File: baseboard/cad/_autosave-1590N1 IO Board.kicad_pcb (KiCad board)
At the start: 4 copper layers, 58 x 77 mm, 105 parts, among them J1 DC POWER JACK, J10 2P_HEADER, J11 2P_HEADER, J12 6-440054-2, J13 6-440054-2, J16 Conn_01x04_Pin, J17 6-440054-2, J18 6-440054-2, J2 1/4" JACK, STEREO, J3 6-440054-2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

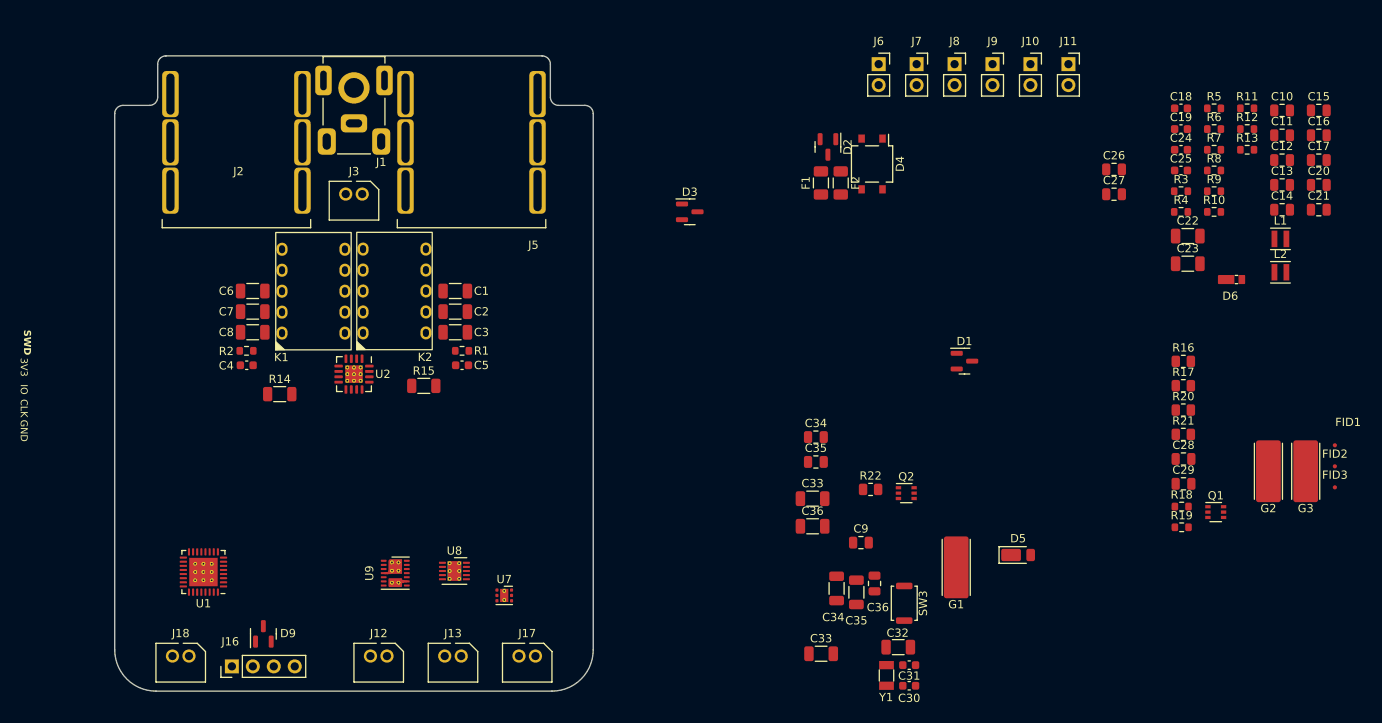
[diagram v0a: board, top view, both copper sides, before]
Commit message: updated schematic page setup
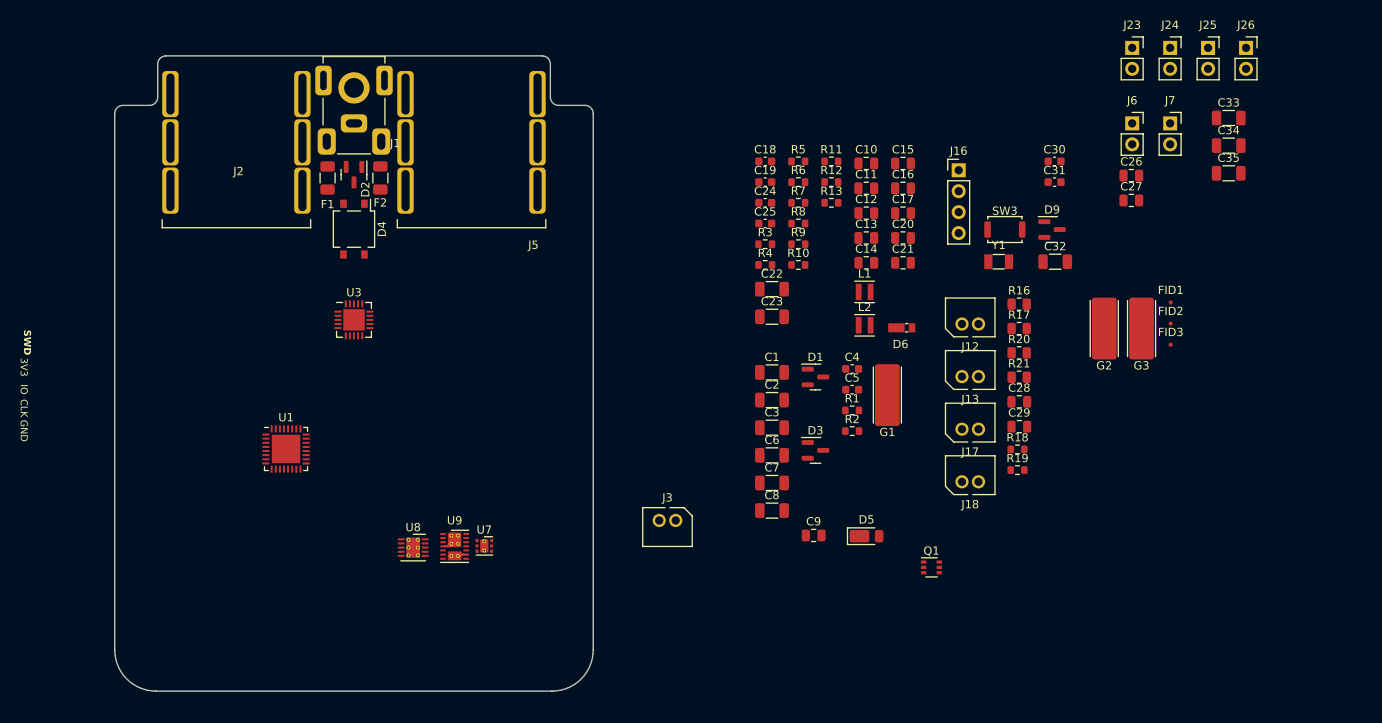
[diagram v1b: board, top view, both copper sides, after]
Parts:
- removed the C33 at (184.6, 141.5)
- removed the C33 at (183.6, 122.7)
- removed the C34 at (186.5, 133.6)
- removed the C34 at (184.0, 115.2)
- removed the C35 at (184.0, 118.2)
- removed the C35 at (188.9, 134.0)
- removed C36: 22μF, Capacitor_SMD:C_0805_2012Metric
- removed C36: 100nF, Capacitor_SMD:C_1206_3216Metric
- removed J10, J11, J8, J9: 2P_HEADER, Connector_PinSocket_2.54mm:PinSocket_1x02_P2.54mm_Vertical
- removed K1, K2: TQ2-L2-3V3, Library:Panasonic_TQ2-L2-5V
- removed Q2: Q_Dual_NMOS_S1G1D2S2G2D1, Package_TO_SOT_SMD:SOT-363_SC-70-6
- removed R14, R15: 0Ω, Resistor_SMD:R_1206_3216Metric
- removed R22: 47Ω, Resistor_SMD:R_0805_2012Metric
- removed U2: DRV8833RTY, Package_DFN_QFN:Texas_S-PWQFN-N16_EP2.1x2.1mm_ThermalVias
- added C33: 100nF, Capacitor_SMD:C_1206_3216Metric, F.Cu at (234.0, 76.5)
- added C34: 100nF, Capacitor_SMD:C_1206_3216Metric, F.Cu at (234.0, 79.9)
- added C35: 100nF, Capacitor_SMD:C_1206_3216Metric, F.Cu at (234.0, 83.2)
- added J23: 2P_HEADER, Connector_PinSocket_2.54mm:PinSocket_1x02_P2.54mm_Vertical, F.Cu at (222.3, 68.0)
- added J24: 2P_HEADER, Connector_PinSocket_2.54mm:PinSocket_1x02_P2.54mm_Vertical, F.Cu at (226.9, 68.0)
- added J25: 2P_HEADER, Connector_PinSocket_2.54mm:PinSocket_1x02_P2.54mm_Vertical, F.Cu at (231.5, 68.0)
- added J26: 2P_HEADER, Connector_PinSocket_2.54mm:PinSocket_1x02_P2.54mm_Vertical, F.Cu at (236.1, 68.0)
- added U3: ADG5434, Package_CSP:LFCSP-20-1EP_4x4mm_P0.5mm_EP2.6x2.6mm, F.Cu at (128.0, 101.0)
- D2: value PESD12VL2BT,215 -> TVS
- U1: footprint Package_DFN_QFN:QFN-32-1EP_5x5mm_P0.5mm_EP3.45x3.45mm_ThermalVias -> Package_DFN_QFN:QFN-32-1EP_5x5mm_P0.5mm_EP3.45x3.45mm
- moved D9 107.4 mm to (212.6, 90.0), turned to 0 degrees
- moved J16 106.7 mm to (201.3, 82.9), turned to 0 degrees
- moved J18 97.3 mm to (202.7, 122.4), turned to 0 degrees
- moved J12 80.6 mm to (202.7, 103.2), turned to 0 degrees
- moved R2 74.1 mm to (188.4, 114.5)
- moved C4 73.4 mm to (188.4, 107.0), turned to 0 degrees
- moved J13 69.7 mm to (202.7, 109.6), turned to 0 degrees
- moved C8 66.6 mm to (178.7, 124.1)
- moved C7 66.3 mm to (178.7, 120.8)
- moved C6 66.0 mm to (178.7, 117.4)
- moved C30 66.0 mm to (212.9, 81.8)
- moved D4 63.3 mm to (128.0, 90.0)
- moved C31 61.1 mm to (212.9, 84.3)
- moved F1 59.8 mm to (124.8, 83.8)
- moved J17 58.8 mm to (202.7, 116.0), turned to 0 degrees
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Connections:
- net /Microcontroller/MCXO1 renamed /Microcontroller/XO1
- net /Microcontroller/MCXO2 renamed /Microcontroller/XO2
- U1 pad 10: /Microcontroller/H-BRIDGE_FAULT -> /Microcontroller/SW_EN
- U1 pad 11: /Microcontroller/H-BRIDGE2_IN2 -> /Microcontroller/SW_IN1
- U1 pad 12: /Microcontroller/H-BRIDGE2_IN1 -> /Microcontroller/SW_IN2
- U1 pad 13: /Microcontroller/H-BRIDGE1_IN2 -> /Microcontroller/SW_IN3
- U1 pad 14: /Microcontroller/H-BRIDGE1_IN1 -> /Microcontroller/SW_IN4
- U1 pad 19: +9V_EN -> unconnected-(U1-PA9/NC-Pad19)
- U1 pad 20: -9V_EN -> unconnected-(U1-PC6-Pad20)
- U1 pad 9: /Microcontroller/H-BRIDGE_SLEEP -> unconnected-(U1-PA2-Pad9)
- U9 pad 10: -9V_EN -> +Vsw
- U9 pad 12: +9V_EN -> +Vsw
